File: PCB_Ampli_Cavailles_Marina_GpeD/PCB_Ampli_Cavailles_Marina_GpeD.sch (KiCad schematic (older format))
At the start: 53 parts, among them J1 AudioJack2_Ground, J2 Conn_01x02, J3 Conn_01x03, Q1 2N2907, Q10 TIP32, Q11 BD138, Q12 TIP31, Q13 2N2222, Q2 2N2907, Q3 2N2907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

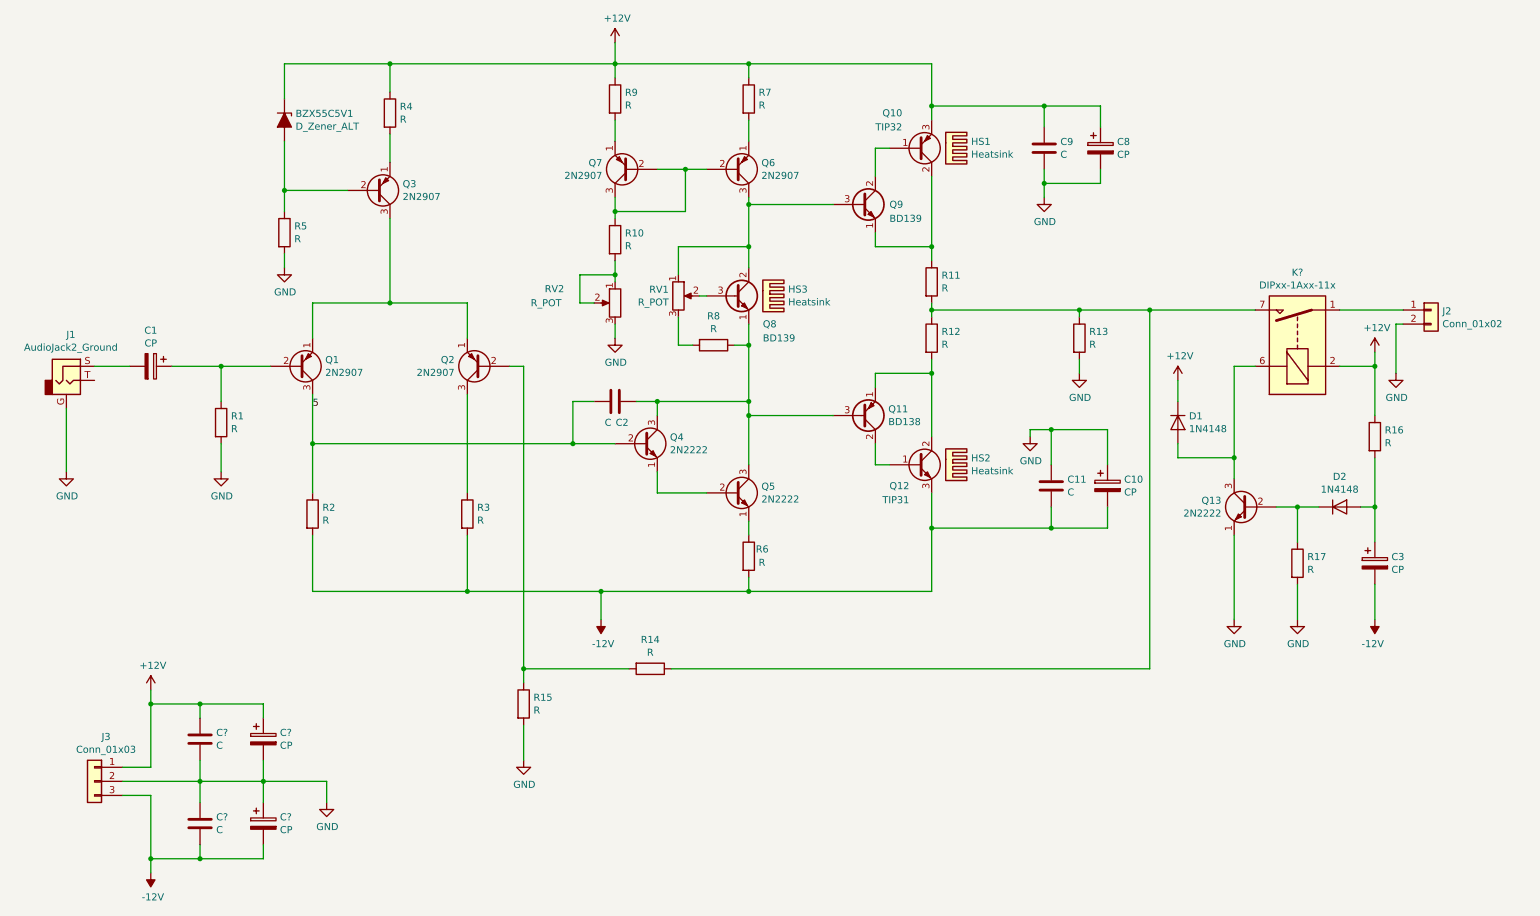
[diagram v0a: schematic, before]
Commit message: Quelques élements associées aux footprints
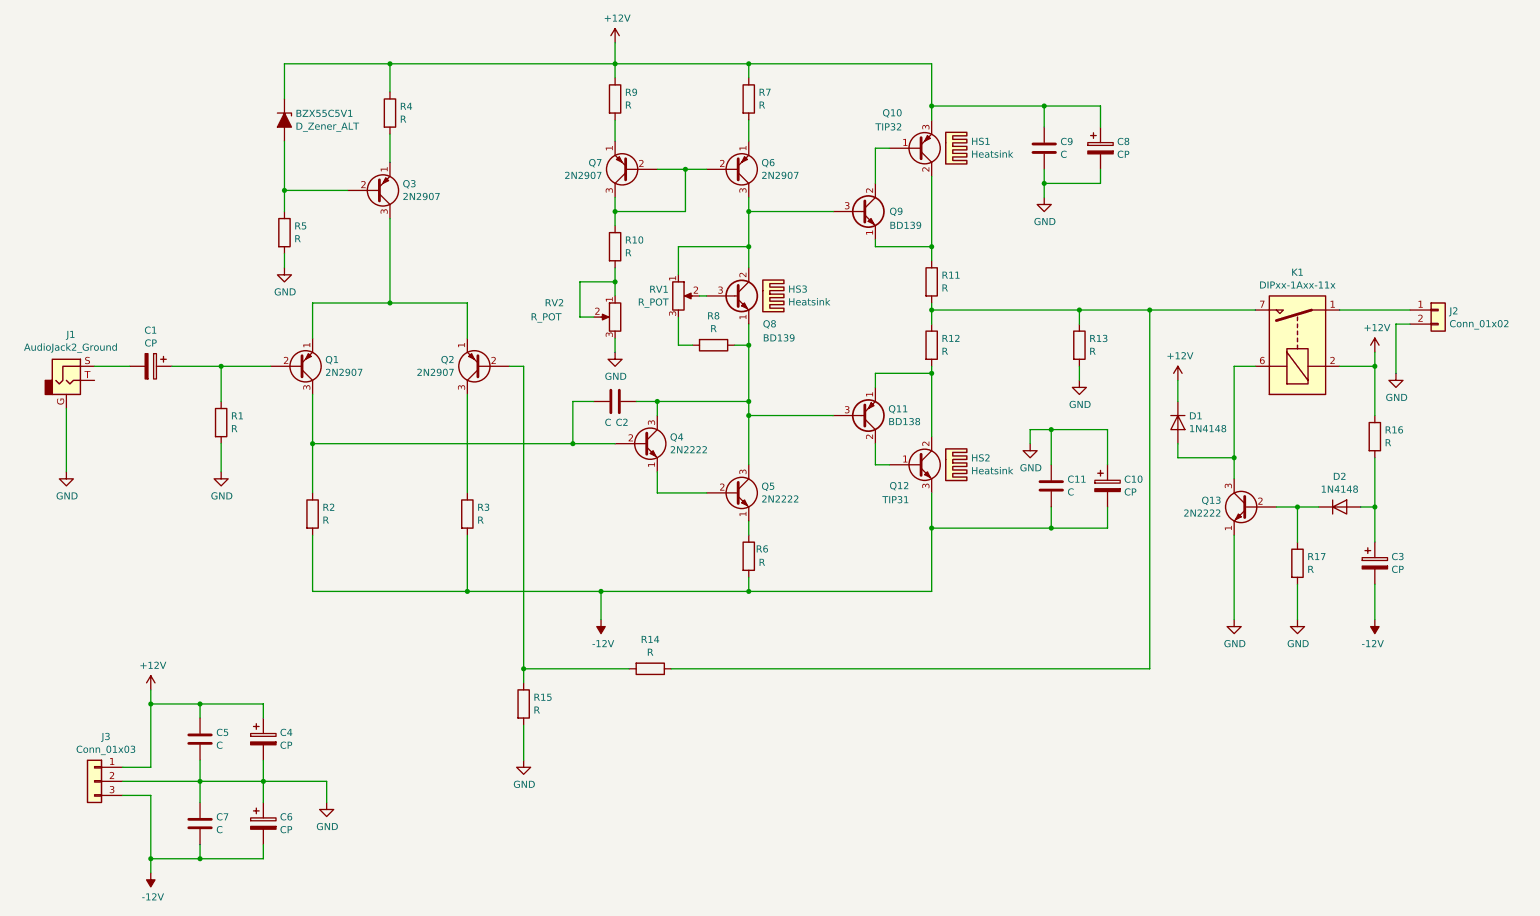
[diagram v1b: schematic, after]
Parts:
- BZX55C5V1: footprint (none) -> CmpAmpliAudio:D_DO-35_SOD27_P10.16mm_Horizontal
- D1, D2: footprint Diode_THT:D_DO-35_SOD27_P7.62mm_Horizontal -> CmpAmpliAudio:D_DO-35_SOD27_P10.16mm_Horizontal
- HS1, HS2, HS3: footprint (none) -> CmpAmpliAudio:Heatsink_Fischer_SK104-STC-STIC_35x13mm_2xDrill2.5mm
- J2: footprint (none) -> CmpAmpliAudio:PhoenixContact_MSTBVA_2,5_2-G-5,08_1x02_P5.08mm_Vertical
- J3: footprint (none) -> CmpAmpliAudio:PhoenixContact_MSTBVA_2,5_3-G-5,08_1x03_P5.08mm_Vertical
- K1: renamed from K?; footprint Relay_THT:Relay_StandexMeder_DIP_LowProfile -> (none)
- Q1, Q13, Q2, Q3, Q4, Q5, Q6, Q7: footprint (none) -> CmpAmpliAudio:TO-18-3
- Q10, Q12: footprint (none) -> CmpAmpliAudio:TO-220-3_Vertical
- Q11, Q8, Q9: footprint Package_TO_SOT_THT:TO-126-3_Vertical -> CmpAmpliAudio:TO-126-3_Vertical
- R1, R10, R13, R14, R15, R16, R17, R2, R3, R4, R5, R6, R7, R8, R9: footprint (none) -> CmpAmpliAudio:R_Axial_DIN0207_L6.3mm_D2.5mm_P10.16mm_Horizontal
- R11, R12: footprint (none) -> CmpAmpliAudio:R_Axial_DIN0516_L15.5mm_D5.0mm_P20.32mm_Horizontal
- RV1, RV2: footprint (none) -> CmpAmpliAudio:Potentiometer_Bourns_3296W_Vertical
- gave numbers to parts that had none: 4
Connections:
- net 5: no longer names the net of C2.2, Q1.3 (C), Q4.2 (B), R2.1
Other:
- moved on the sheet: J2, Q9, R10, R12, R13, RV2

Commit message: Nouvelles associations de footprints
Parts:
- C1, C10, C3, C4, C6, C8: footprint (none) -> CmpAmpliAudio:CP_Radial_D8.0mm_P5.00mm
- C11, C2, C5, C7, C9: footprint (none) -> CmpAmpliAudio:C_Rect_L7.2mm_W3.5mm_P5.00mm_FKS2_FKP2_MKS2_MKP2
- J1: footprint (none) -> CmpAmpliAudio:Jack_35RAPC2AV
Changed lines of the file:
@@
 F 0 "C1" V 1245 3700 50  0000 C CNN
 F 1 "CP" V 1336 3700 50  0000 C CNN
-F 2 "" H 1538 3550 50  0001 C CNN
+F 2 "CmpAmpliAudio:CP_Radial_D8.0mm_P5.00mm" H 1538 3550 50  0001 C CNN
 F 3 "~" H 1500 3700 50  0001 C CNN
 	1    1500 3700
@@
 F 0 "C2" V 4950 4000 50  0000 C CNN
 F 1 "C" V 4950 3900 50  0000 C CNN
-F 2 "" H 4838 3800 50  0001 C CNN
+F 2 "CmpAmpliAudio:C_Rect_L7.2mm_W3.5mm_P5.00mm_FKS2_FKP2_MKS2_MKP2" H 4838 3800 50  0001 C CNN
 F 3 "~" H 4800 3950 50  0001 C CNN
 	1    4800 3950
@@
 F 0 "C9" H 7965 2196 50  0000 L CNN
 F 1 "C" H 7965 2105 50  0000 L CNN
-F 2 "" H 7888 2000 50  0001 C CNN
+F 2 "CmpAmpliAudio:C_Rect_L7.2mm_W3.5mm_P5.00mm_FKS2_FKP2_MKS2_MKP2" H 7888 2000 50  0001 C CNN
 F 3 "~" H 7850 2150 50  0001 C CNN
 	1    7850 2150
@@
 F 0 "C8" H 8368 2196 50  0000 L CNN
 F 1 "CP" H 8368 2105 50  0000 L CNN
-F 2 "" H 8288 2000 50  0001 C CNN
+F 2 "CmpAmpliAudio:CP_Radial_D8.0mm_P5.00mm" H 8288 2000 50  0001 C CNN
 F 3 "~" H 8250 2150 50  0001 C CNN
 	1    8250 2150
@@
 F 0 "C11" H 8015 4596 50  0000 L CNN
 F 1 "C" H 8015 4505 50  0000 L CNN
-F 2 "" H 7938 4400 50  0001 C CNN
+F 2 "CmpAmpliAudio:C_Rect_L7.2mm_W3.5mm_P5.00mm_FKS2_FKP2_MKS2_MKP2" H 7938 4400 50  0001 C CNN
 F 3 "~" H 7900 4550 50  0001 C CNN
 	1    7900 4550
@@
 F 0 "C10" H 8418 4596 50  0000 L CNN
 F 1 "CP" H 8418 4505 50  0000 L CNN
-F 2 "" H 8338 4400 50  0001 C CNN
+F 2 "CmpAmpliAudio:CP_Radial_D8.0mm_P5.00mm" H 8338 4400 50  0001 C CNN
 F 3 "~" H 8300 4550 50  0001 C CNN
 	1    8300 4550
@@
 F 0 "J1" H 932 4125 50  0000 C CNN
 F 1 "AudioJack2_Ground" H 932 4034 50  0000 C CNN
-F 2 "" H 900 3800 50  0001 C CNN
+F 2 "CmpAmpliAudio:Jack_35RAPC2AV" H 900 3800 50  0001 C CNN
 F 3 "~" H 900 3800 50  0001 C CNN
 	1    900  3800
@@
 F 0 "C5" H 1965 6396 50  0000 L CNN
 F 1 "C" H 1965 6305 50  0000 L CNN
-F 2 "" H 1888 6200 50  0001 C CNN
+F 2 "CmpAmpliAudio:C_Rect_L7.2mm_W3.5mm_P5.00mm_FKS2_FKP2_MKS2_MKP2" H 1888 6200 50  0001 C CNN
 F 3 "~" H 1850 6350 50  0001 C CNN
 	1    1850 6350
@@
 F 0 "C7" H 1965 6996 50  0000 L CNN
 F 1 "C" H 1965 6905 50  0000 L CNN
-F 2 "" H 1888 6800 50  0001 C CNN
+F 2 "CmpAmpliAudio:C_Rect_L7.2mm_W3.5mm_P5.00mm_FKS2_FKP2_MKS2_MKP2" H 1888 6800 50  0001 C CNN
 F 3 "~" H 1850 6950 50  0001 C CNN
 	1    1850 6950
@@
 F 0 "C4" H 2418 6396 50  0000 L CNN
 F 1 "CP" H 2418 6305 50  0000 L CNN
-F 2 "" H 2338 6200 50  0001 C CNN
+F 2 "CmpAmpliAudio:CP_Radial_D8.0mm_P5.00mm" H 2338 6200 50  0001 C CNN
 F 3 "~" H 2300 6350 50  0001 C CNN
 	1    2300 6350
@@
 F 0 "C6" H 2418 6996 50  0000 L CNN
 F 1 "CP" H 2418 6905 50  0000 L CNN
-F 2 "" H 2338 6800 50  0001 C CNN
+F 2 "CmpAmpliAudio:CP_Radial_D8.0mm_P5.00mm" H 2338 6800 50  0001 C CNN
 F 3 "~" H 2300 6950 50  0001 C CNN
 	1    2300 6950
@@
 F 0 "C3" H 10318 5146 50  0000 L CNN
 F 1 "CP" H 10318 5055 50  0000 L CNN
-F 2 "" H 10238 4950 50  0001 C CNN
+F 2 "CmpAmpliAudio:CP_Radial_D8.0mm_P5.00mm" H 10238 4950 50  0001 C CNN
 F 3 "~" H 10200 5100 50  0001 C CNN
 	1    10200 5100

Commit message: PCB Modifié
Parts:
- removed HS3: Heatsink, CmpAmpliAudio:Heatsink_Fischer_SK104-STC-STIC_35x13mm_2xDrill2.5mm, symbol Mechanical:Heatsink
- removed J1: AudioJack2_Ground, CmpAmpliAudio:Jack_35RAPC2AV, symbol Connector:AudioJack2_Ground
- removed K1: DIPxx-1Axx-11x, symbol Relay:DIPxx-1Axx-11x
- added U1: Relay_1CT, CmpAmpliAudioTR:Relais_112LMH2, symbol CmpAmpliAudioTR:Relay_1CT
- added U2: Jack_Mono, CmpAmpliAudioTR:Jack_35RAPC2AV, symbol CmpAmpliAudioTR:Jack_Mono
- C1, C3: value CP -> 47u
- C10, C8: value CP -> 470u; footprint CmpAmpliAudio:CP_Radial_D8.0mm_P5.00mm -> CmpAmpliAudioTR:CP_Radial_D12.5mm_P5.00mm
- C11, C5, C7, C9: value C -> 100n
- C4, C6: value CP -> 10u
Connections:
- net +12V: now also U1.b2
- net GND: now also U2.G
- net at C1.2: now also U2.TN
- net at R11.2, R12.1, R13.1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: now also U1.c1
- net at J2.1 (Pin_1): now also U1.c2
- net at D1.2 (A), Q13.3 (C): now also U1.b1
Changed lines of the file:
@@
 encoding utf-8
 Sheet 1 1
-Title ""
-Date ""
-Rev ""
-Comp ""
+Title "PCB - Amplificateur d'audio"
+Date "08/04/2020"
+Rev "V0"
+Comp "INSA GEI"
 Comment1 ""
 Comment2 ""
@@
 P 1500 3700
 F 0 "C1" V 1245 3700 50  0000 C CNN
-F 1 "CP" V 1336 3700 50  0000 C CNN
+F 1 "47u" V 1336 3700 50  0000 C CNN
 F 2 "CmpAmpliAudio:CP_Radial_D8.0mm_P5.00mm" H 1538 3550 50  0001 C CNN
 F 3 "~" H 1500 3700 50  0001 C CNN
@@
 $EndComp
 Wire Wire Line
-	4150 6250 4150 6500
-$Comp
-L Mechanical:Heatsink HS3
-U 1 1 5E7D9CCB
-P 5850 3200
-F 0 "HS3" V 5803 3380 50  0000 L CNN
-F 1 "Heatsink" V 5894 3380 50  0000 L CNN
-F 2 "CmpAmpliAudio:Heatsink_Fischer_SK104-STC-STIC_35x13mm_2xDrill2.5mm" H 5862 3200 50  0001 C CNN
-F 3 "~" H 5862 3200 50  0001 C CNN
-	1    5850 3200
-	0    1    1    0
-$EndComp
+	4150 6250 4150 6400
 $Comp
 L Device:R_POT RV1
@@
 P 7850 2150
 F 0 "C9" H 7965 2196 50  0000 L CNN
-F 1 "C" H 7965 2105 50  0000 L CNN
+F 1 "100n" H 7965 2105 50  0000 L CNN
 F 2 "CmpAmpliAudio:C_Rect_L7.2mm_W3.5mm_P5.00mm_FKS2_FKP2_MKS2_MKP2" H 7888 2000 50  0001 C CNN
 F 3 "~" H 7850 2150 50  0001 C CNN
@@
 P 8250 2150
 F 0 "C8" H 8368 2196 50  0000 L CNN
-F 1 "CP" H 8368 2105 50  0000 L CNN
-F 2 "CmpAmpliAudio:CP_Radial_D8.0mm_P5.00mm" H 8288 2000 50  0001 C CNN
+F 1 "470u" H 8368 2105 50  0000 L CNN
+F 2 "CmpAmpliAudioTR:CP_Radial_D12.5mm_P5.00mm" H 8288 2000 50  0001 C CNN
 F 3 "~" H 8250 2150 50  0001 C CNN
 	1    8250 2150
@@
 P 7900 4550
 F 0 "C11" H 8015 4596 50  0000 L CNN
-F 1 "C" H 8015 4505 50  0000 L CNN
+F 1 "100n" H 8015 4505 50  0000 L CNN
 F 2 "CmpAmpliAudio:C_Rect_L7.2mm_W3.5mm_P5.00mm_FKS2_FKP2_MKS2_MKP2" H 7938 4400 50  0001 C CNN
 F 3 "~" H 7900 4550 50  0001 C CNN
@@
 P 8300 4550
 F 0 "C10" H 8418 4596 50  0000 L CNN
-F 1 "CP" H 8418 4505 50  0000 L CNN
-F 2 "CmpAmpliAudio:CP_Radial_D8.0mm_P5.00mm" H 8338 4400 50  0001 C CNN
+F 1 "470u" H 8418 4505 50  0000 L CNN
+F 2 "CmpAmpliAudioTR:CP_Radial_D12.5mm_P5.00mm" H 8338 4400 50  0001 C CNN
 F 3 "~" H 8300 4550 50  0001 C CNN
 	1    8300 4550
@@
 Connection ~ 8100 3300
 $Comp
-L Connector:AudioJack2_Ground J1
-U 1 1 5E88DE60
-P 900 3800
-F 0 "J1" H 932 4125 50  0000 C CNN
-F 1 "AudioJack2_Ground" H 932 4034 50  0000 C CNN
-F 2 "CmpAmpliAudio:Jack_35RAPC2AV" H 900 3800 50  0001 C CNN
-F 3 "~" H 900 3800 50  0001 C CNN
-	1    900  3800
-	1    0    0    -1
-$EndComp
-$Comp
 L power:GND #PWR0110
 U 1 1 5E891E9F
-P 900 4450
-F 0 "#PWR0110" H 900 4200 50  0001 C CNN
-F 1 "GND" H 905 4277 50  0000 C CNN
-F 2 "" H 900 4450 50  0001 C CNN
-F 3 "" H 900 4450 50  0001 C CNN
-	1    900  4450
+P 800 4400
+F 0 "#PWR0110" H 800 4150 50  0001 C CNN
+F 1 "GND" H 805 4227 50  0000 C CNN
+F 2 "" H 800 4400 50  0001 C CNN
+F 3 "" H 800 4400 50  0001 C CNN
+	1    800  4400
 	1    0    0    -1
 $EndComp
@@
 P 1850 6350
 F 0 "C5" H 1965 6396 50  0000 L CNN
-F 1 "C" H 1965 6305 50  0000 L CNN
+F 1 "100n" H 1965 6305 50  0000 L CNN
 F 2 "CmpAmpliAudio:C_Rect_L7.2mm_W3.5mm_P5.00mm_FKS2_FKP2_MKS2_MKP2" H 1888 6200 50  0001 C CNN
 F 3 "~" H 1850 6350 50  0001 C CNN
@@
 P 1850 6950
 F 0 "C7" H 1965 6996 50  0000 L CNN
-F 1 "C" H 1965 6905 50  0000 L CNN
+F 1 "100n" H 1965 6905 50  0000 L CNN
 F 2 "CmpAmpliAudio:C_Rect_L7.2mm_W3.5mm_P5.00mm_FKS2_FKP2_MKS2_MKP2" H 1888 6800 50  0001 C CNN
 F 3 "~" H 1850 6950 50  0001 C CNN
@@
 P 2300 6350
 F 0 "C4" H 2418 6396 50  0000 L CNN
-F 1 "CP" H 2418 6305 50  0000 L CNN
+F 1 "10u" H 2418 6305 50  0000 L CNN
 F 2 "CmpAmpliAudio:CP_Radial_D8.0mm_P5.00mm" H 2338 6200 50  0001 C CNN
 F 3 "~" H 2300 6350 50  0001 C CNN
@@
 P 2300 6950
 F 0 "C6" H 2418 6996 50  0000 L CNN
-F 1 "CP" H 2418 6905 50  0000 L CNN
+F 1 "10u" H 2418 6905 50  0000 L CNN
 F 2 "CmpAmpliAudio:CP_Radial_D8.0mm_P5.00mm" H 2338 6800 50  0001 C CNN
 F 3 "~" H 2300 6950 50  0001 C CNN
@@
 Wire Wire Line
 	1850 7200 2300 7200
-$Comp
-L Relay:DIPxx-1Axx-11x K1
-U 1 1 5E8F41C6
-P 9650 3500
-F 0 "K1" V 10117 3500 50  0000 C CNN
-F 1 "DIPxx-1Axx-11x" V 10026 3500 50  0000 C CNN
-F 2 "" H 10000 3450 50  0001 L CNN
-F 3 "https://standexelectronics.com/wp-content/uploads/datasheet_reed_relay_DIP.pdf" H 9650 3500 50  0001 C CNN
-	1    9650 3500
-	0    -1   -1   0
-$EndComp
 Wire Wire Line
 	8600 3300 9350 3300
@@
 P 10200 5100
 F 0 "C3" H 10318 5146 50  0000 L CNN
-F 1 "CP" H 10318 5055 50  0000 L CNN
+F 1 "47u" H 10318 5055 50  0000 L CNN
 F 2 "CmpAmpliAudio:CP_Radial_D8.0mm_P5.00mm" H 10238 4950 50  0001 C CNN
 F 3 "~" H 10200 5100 50  0001 C CNN
@@
 Connection ~ 1500 7200
 Wire Wire Line
-	900  4450 900  4000
-Wire Wire Line
-	10200 5250 10200 5500
+	800  4400 800  3950
+Wire Wire Line
+	10200 5250 10200 5400
 $Comp
 L Device:Q_PNP_BCE Q10
@@
 	1    0    0    -1
 $EndComp
+$Comp
+L CmpAmpliAudioTR:Jack_Mono U2
+U 1 1 5E8F30F4
+P 900 3700
+F 0 "U2" H 928 3967 50  0000 C CNN
+F 1 "Jack_Mono" H 928 3876 50  0000 C CNN
+F 2 "CmpAmpliAudioTR:Jack_35RAPC2AV" H 950 3900 50  0001 C CNN
+F 3 "" H 950 3900 50  0001 C CNN
+	1    900  3700
+	1    0    0    -1
+$EndComp
+$Comp
+L CmpAmpliAudioTR:Relay_1CT U1
+U 1 1 5E8EC916
+P 9650 3500
+F 0 "U1" V 10117 3500 50  0000 C CNN
+F 1 "Relay_1CT" V 10026 3500 50  0000 C CNN
+F 2 "CmpAmpliAudioTR:Relais_112LMH2" H 9650 3500 50  0001 C CNN
+F 3 "" H 9650 3500 50  0001 C CNN
+	1    9650 3500
+	0    -1   -1   0
+$EndComp
+$Comp
+L power:PWR_FLAG #FLG0101
+U 1 1 5E91F68E
+P 1450 6100
+F 0 "#FLG0101" H 1450 6175 50  0001 C CNN
+F 1 "PWR_FLAG" V 1450 6227 50  0000 L CNN
+F 2 "" H 1450 6100 50  0001 C CNN
+F 3 "~" H 1450 6100 50  0001 C CNN
+	1    1450 6100
+	0    -1   -1   0
+$EndComp
+Wire Wire Line
+	1450 6100 1500 6100
+$Comp
+L power:PWR_FLAG #FLG0102
+U 1 1 5E94D079
+P 10400 5400
+F 0 "#FLG0102" H 10400 5475 50  0001 C CNN
+F 1 "PWR_FLAG" V 10400 5528 50  0000 L CNN
+F 2 "" H 10400 5400 50  0001 C CNN
+F 3 "~" H 10400 5400 50  0001 C CNN
+	1    10400 5400
+	0    1    1    0
+$EndComp
+Wire Wire Line
+	10400 5400 10200 5400
+Connection ~ 10200 5400
+Wire Wire Line
+	10200 5400 10200 5500
+$Comp
+L power:PWR_FLAG #FLG0103
+U 1 1 5E962DAE
+P 4150 6400
+F 0 "#FLG0103" H 4150 6475 50  0001 C CNN
+F 1 "PWR_FLAG" V 4150 6527 50  0000 L CNN
+F 2 "" H 4150 6400 50  0001 C CNN
+F 3 "~" H 4150 6400 50  0001 C CNN
+	1    4150 6400
+	0    -1   -1   0
+$EndComp
+Connection ~ 4150 6400
+Wire Wire Line
+	4150 6400 4150 6500
 $EndSCHEMATC

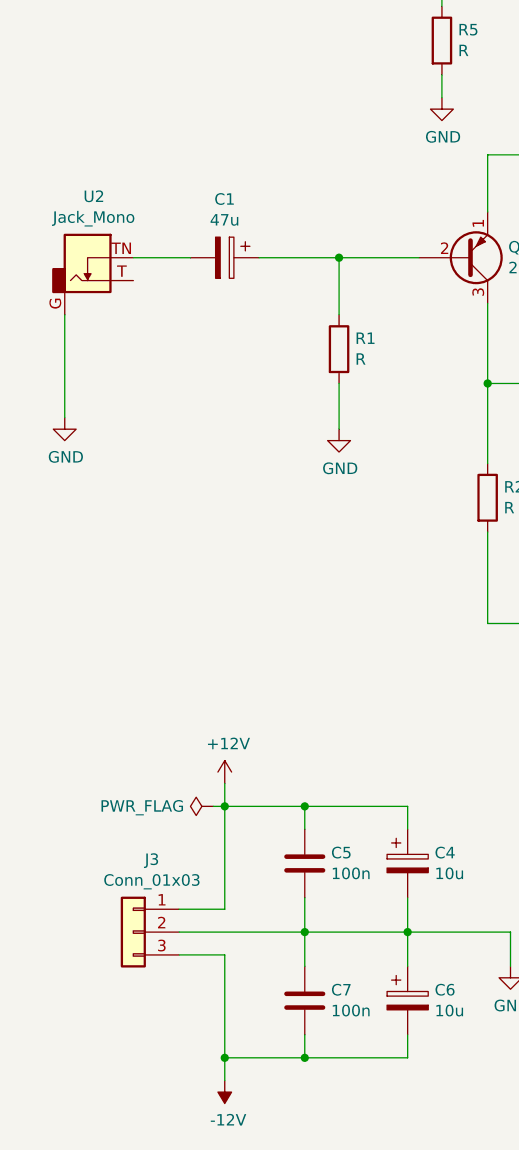
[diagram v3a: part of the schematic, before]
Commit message: Cambiadas las orientaciones de las alimentaciones y la salida
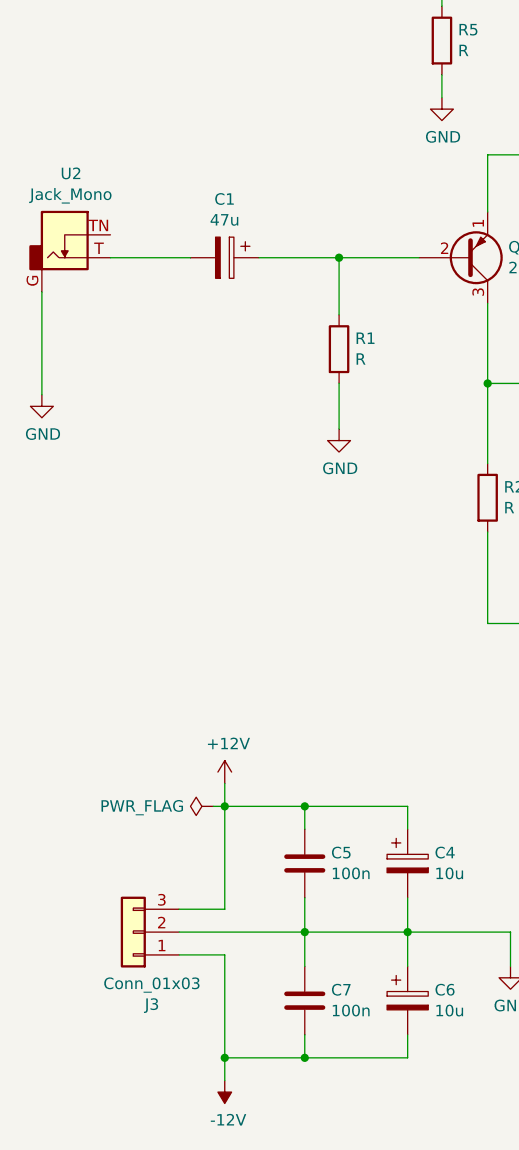
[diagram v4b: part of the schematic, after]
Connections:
- net +12V: now also J3.3 (Pin_3); no longer J3.1 (Pin_1)
- net -12V: now also J3.1 (Pin_1); no longer J3.3 (Pin_3)
- net at C1.2: now also U2.T; no longer U2.TN
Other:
- moved on the sheet: U2

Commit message: Nouvelle PCB
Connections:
- net +12V: now also U1.b1; no longer U1.b2
- net GND: now also J2.1 (Pin_1); no longer J2.2 (Pin_2)
- net at R11.2, R12.1, R13.1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: now also U1.c2; no longer U1.c1
- net at D1.2 (A), Q13.3 (C): now also U1.b2; no longer U1.b1
- new net: J2.2 (Pin_2), U1.c1
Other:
- moved on the sheet: J2
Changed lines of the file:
@@
 Wire Wire Line
 	1850 7200 2300 7200
-Wire Wire Line
-	8600 3300 9350 3300
-Connection ~ 8600 3300
 $Comp
 L Device:Q_NPN_EBC Q13
@@
 	-1   0    0    -1
 $EndComp
-Wire Wire Line
-	9350 3700 9200 3700
 $Comp
 L Diode:1N4148 D1
@@
 Wire Wire Line
 	10200 4700 10200 4350
-Wire Wire Line
-	10200 4050 10200 3700
-Wire Wire Line
-	10200 3700 9950 3700
 $Comp
 L power:+12V #PWR0118
@@
 	1    0    0    -1
 $EndComp
-Wire Wire Line
-	10200 3600 10200 3700
-Connection ~ 10200 3700
-Wire Wire Line
-	10450 3300 9950 3300
 $Comp
 L power:GND #PWR0119
@@
 	1    0    0    -1
 $EndComp
-Wire Wire Line
-	10450 3400 10350 3400
 Wire Wire Line
 	10350 3400 10350 3750
@@
 L Connector_Generic:Conn_01x02 J2
 U 1 1 5E920633
-P 10650 3300
-F 0 "J2" H 10730 3292 50  0000 L CNN
-F 1 "Conn_01x02" H 10730 3201 50  0000 L CNN
-F 2 "CmpAmpliAudio:PhoenixContact_MSTBVA_2,5_2-G-5,08_1x02_P5.08mm_Vertical" H 10650 3300 50  0001 C CNN
-F 3 "~" H 10650 3300 50  0001 C CNN
-	1    10650 3300
-	1    0    0    -1
+P 10700 3400
+F 0 "J2" H 10780 3392 50  0000 L CNN
+F 1 "Conn_01x02" H 10780 3301 50  0000 L CNN
+F 2 "CmpAmpliAudio:PhoenixContact_MSTBVA_2,5_2-G-5,08_1x02_P5.08mm_Vertical" H 10700 3400 50  0001 C CNN
+F 3 "~" H 10700 3400 50  0001 C CNN
+	1    10700 3400
+	1    0    0    1
 $EndComp
 $Comp
@@
 F 3 "" H 9650 3500 50  0001 C CNN
 	1    9650 3500
-	0    -1   -1   0
+	0    1    -1   0
 $EndComp
 $Comp
@@
 Wire Wire Line
 	1300 6750 1500 6750
+Wire Wire Line
+	10500 3400 10350 3400
+Wire Wire Line
+	10200 3600 10200 3700
+Wire Wire Line
+	9350 3300 8600 3300
+Connection ~ 8600 3300
+Wire Wire Line
+	9950 3300 10500 3300
+Wire Wire Line
+	9350 3700 9200 3700
+Wire Wire Line
+	9950 3700 10200 3700
+Connection ~ 10200 3700
+Wire Wire Line
+	10200 3700 10200 4050
 $EndSCHEMATC
